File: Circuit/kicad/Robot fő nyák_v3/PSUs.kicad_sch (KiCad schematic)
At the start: 42 parts, among them U46 AP64501SP-13, U47 AP64501SP-13, U48 AP64501SP-13

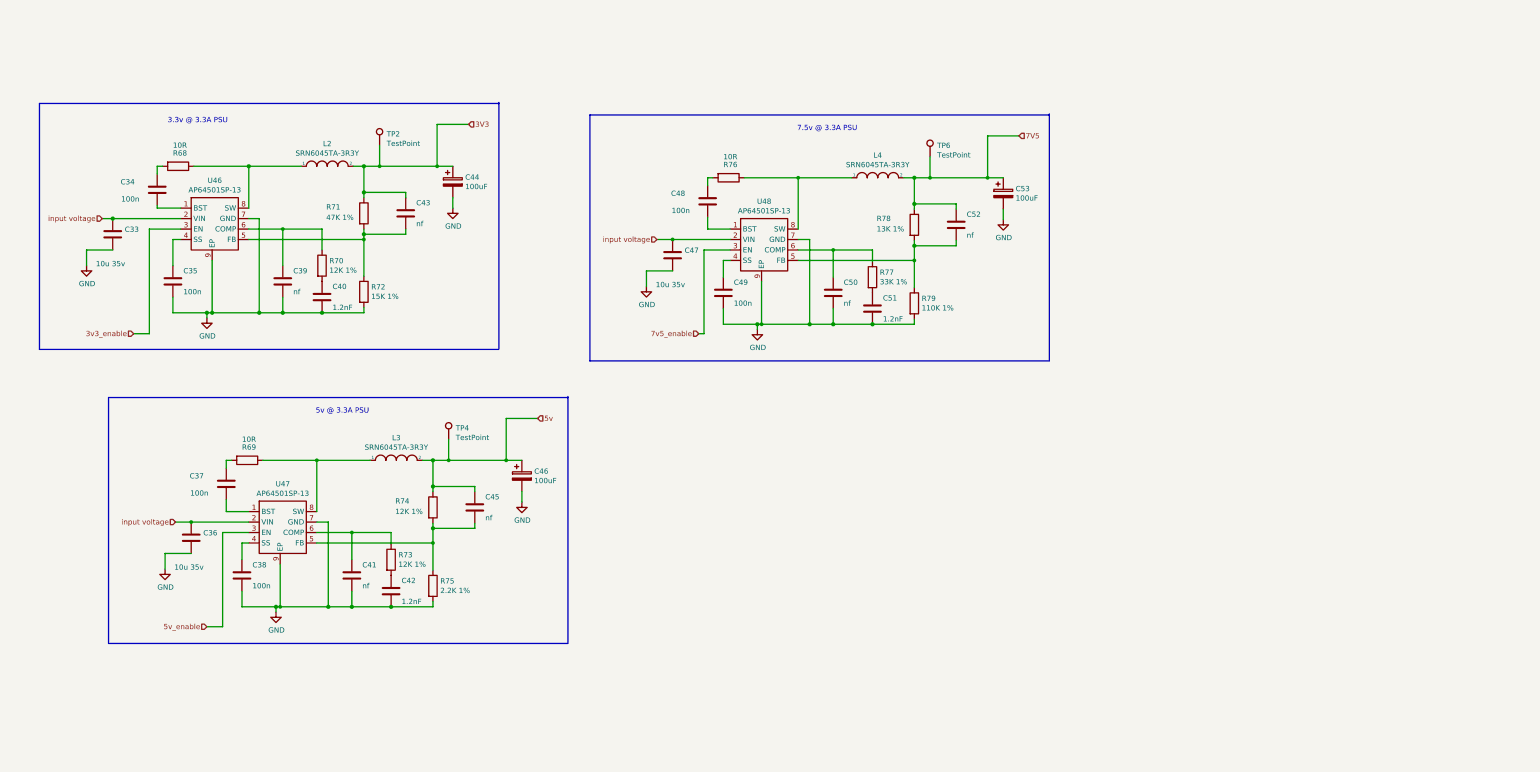
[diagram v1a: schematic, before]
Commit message: kicad bugfixs + bno085 + level shifter ics
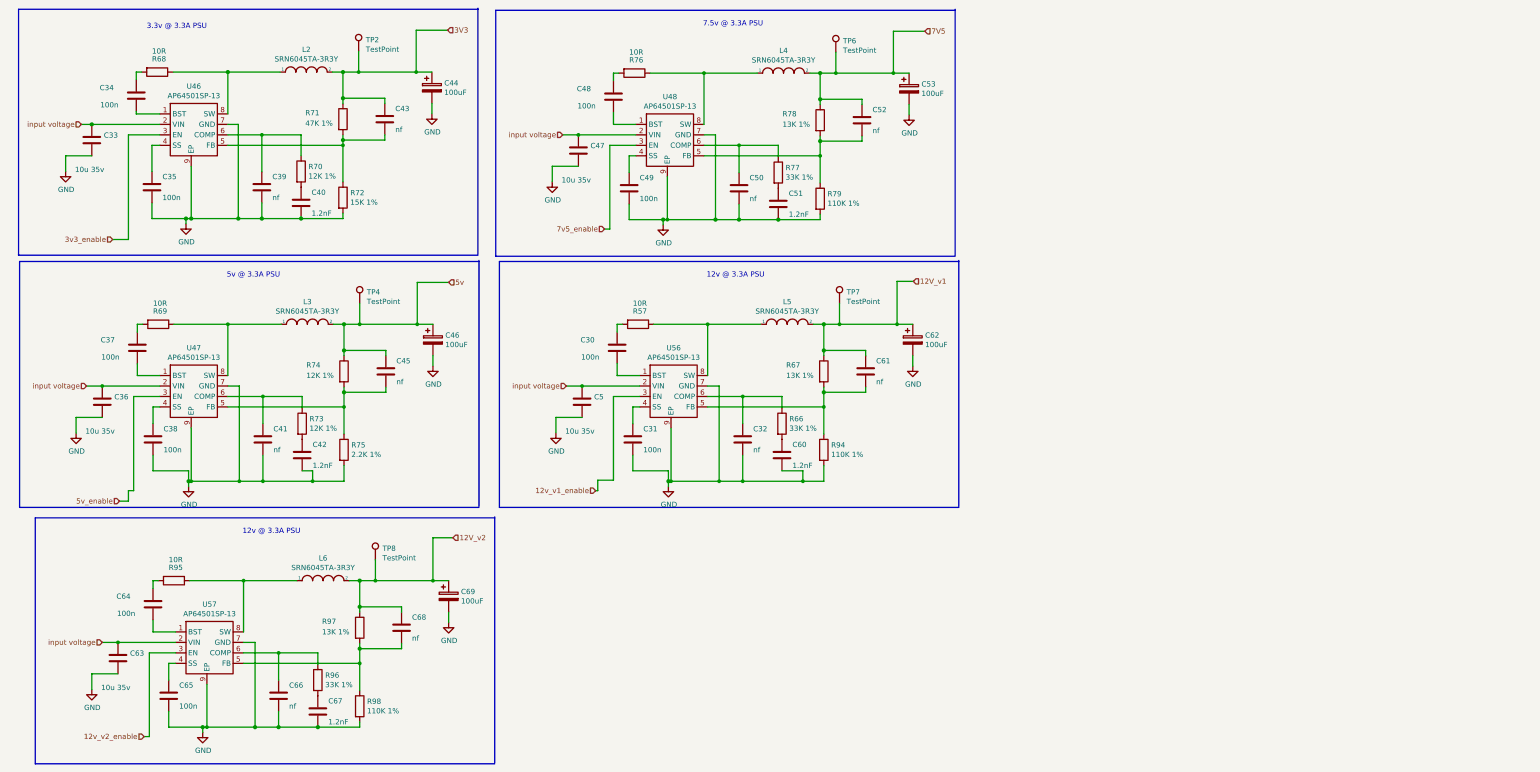
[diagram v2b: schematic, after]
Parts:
- added C30, C31, C64, C65: 100n, Capacitor_SMD:C_0805_2012Metric, symbol Device:C
- added C32, C61, C66, C68: nf, Capacitor_SMD:C_0805_2012Metric, symbol Device:C
- added C5, C63: 10u 35v, Capacitor_SMD:C_0805_2012Metric, symbol Device:C
- added C60, C67: 1.2nF, Capacitor_SMD:C_0805_2012Metric, symbol Device:C
- added C62, C69: 100uF, Capacitor_Tantalum_SMD:CP_EIA-7343-31_Kemet-D, symbol Device:CP
- added L5, L6: SRN6045TA-3R3Y, Inductor_SMD:L_Bourns_SRN6045TA, symbol pspice:INDUCTOR
- added R57, R95: 10R, Resistor_SMD:R_0805_2012Metric_Pad1.20x1.40mm_HandSolder, symbol Device:R
- added R66, R96: 33K 1%, Resistor_SMD:R_0805_2012Metric_Pad1.20x1.40mm_HandSolder, symbol Device:R
- added R67, R97: 13K 1%, Resistor_SMD:R_0805_2012Metric_Pad1.20x1.40mm_HandSolder, symbol Device:R
- added R94, R98: 110K 1%, Resistor_SMD:R_0805_2012Metric_Pad1.20x1.40mm_HandSolder, symbol Device:R
- added TP7, TP8: TestPoint, TestPoint:TestPoint_Pad_1.0x1.0mm, symbol Connector:TestPoint
- added U56, U57: AP64501SP-13, Package_SO:SOIC-8-1EP_3.9x4.9mm_P1.27mm_EP2.95x4.9mm_Mask2.71x3.4mm_ThermalVias, symbol CM4IO:AP64351
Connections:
- net GND: now also C31.2, C32.2, C5.2, C60.2, C62.2, C63.2, C65.2, C66.2, C67.2, C69.2, R94.2, R98.2, U56.7 (GND), U56.9 (EP), U57.7 (GND), U57.9 (EP)
- net input voltage: now also C5.1, C63.1, U56.2 (VIN), U57.2 (VIN)
- new net: L5.1, R57.1, U56.8 (SW)
- new net: C30.1, R57.2
- new net: C30.2, U56.1 (BST)
- new net: C31.1, U56.4 (SS)
- new net: C61.2, R67.2, R94.1, U56.5 (FB)
- new net: C32.1, R66.1, U56.6 (COMP)
- new net: L6.1, R95.1, U57.8 (SW)
- new net: C64.1, R95.2
- new net: C65.1, U57.4 (SS)
- new net: C64.2, U57.1 (BST)
- new net: C68.2, R97.2, R98.1, U57.5 (FB)
- new net: C66.1, R96.1, U57.6 (COMP)
- new net: C67.1, R96.2
- new net: C60.1, R66.2
- new net 12V_v1: C61.1, C62.1, L5.2, R67.1, TP7.1
- new net 12V_v2: C68.1, C69.1, L6.2, R97.1, TP8.1
- new net 12v_v1_enable: U56.3 (EN)
- new net 12v_v2_enable: U57.3 (EN)
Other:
- note added: "12v @ 3.3A PSU"
- moved on the sheet: C33, C34, C35, C36, C37, C38, C39, C40, C41, C42, C43, C44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

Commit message: KICAD V3.01 Cleaned sheets + update + szekér modell add
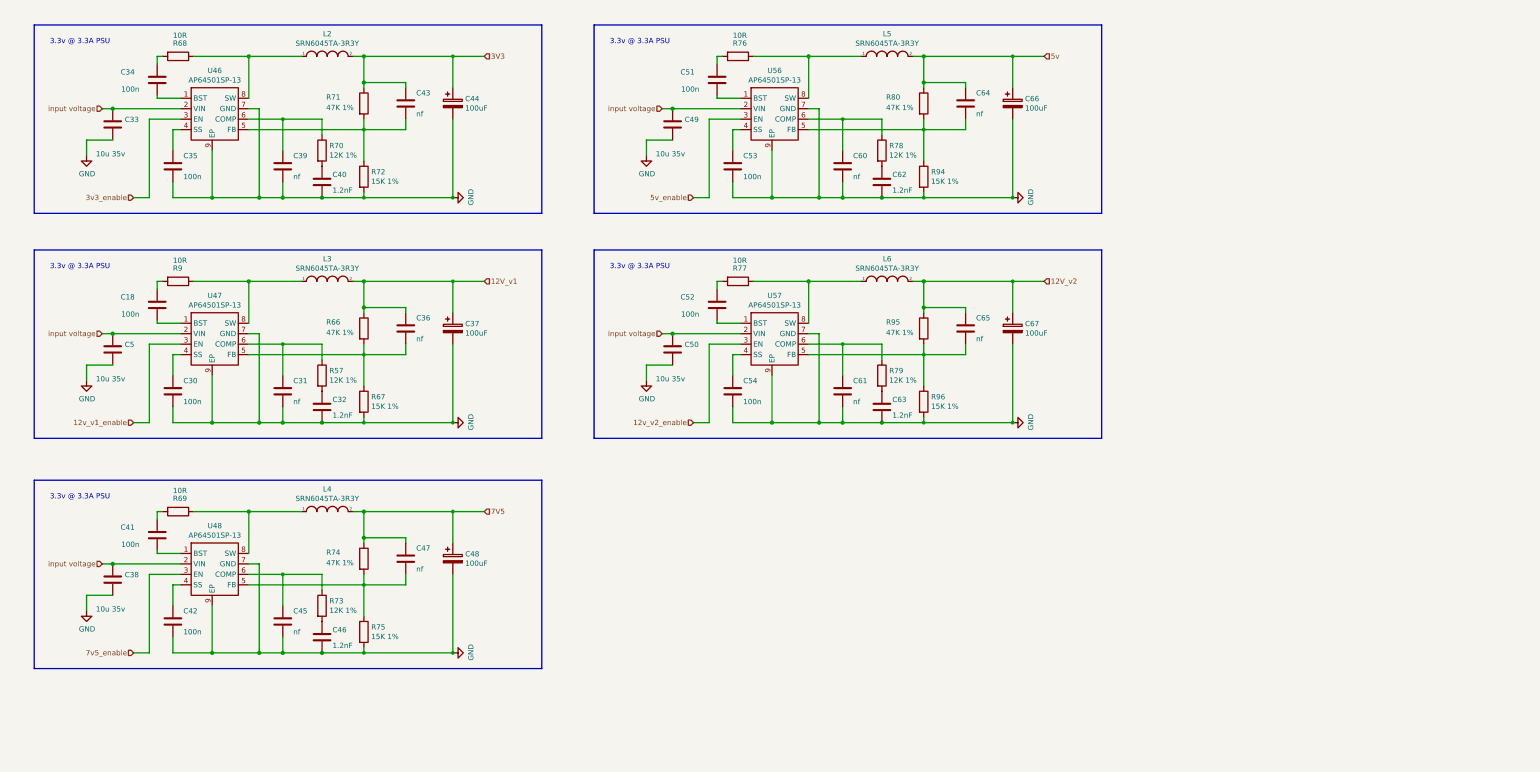
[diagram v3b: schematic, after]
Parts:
- removed C37, C48: 100n, Capacitor_SMD:C_0805_2012Metric, symbol Device:C
- removed C46, C53, C62, C69: 100uF, Capacitor_Tantalum_SMD:CP_EIA-7343-31_Kemet-D, symbol Device:CP
- removed C66, C68: nf, Capacitor_SMD:C_0805_2012Metric, symbol Device:C
- removed C67: 1.2nF, Capacitor_SMD:C_0805_2012Metric, symbol Device:C
- removed R97: 13K 1%, Resistor_SMD:R_0805_2012Metric_Pad1.20x1.40mm_HandSolder, symbol Device:R
- removed R98: 110K 1%, Resistor_SMD:R_0805_2012Metric_Pad1.20x1.40mm_HandSolder, symbol Device:R
- removed TP2, TP4, TP6, TP7, TP8: TestPoint, TestPoint:TestPoint_Pad_1.0x1.0mm, symbol Connector:TestPoint
- added C18, C53, C54: 100n, Capacitor_SMD:C_0805_2012Metric, symbol Device:C
- added C37, C48, C66, C67: 100uF, Capacitor_Tantalum_SMD:CP_EIA-7343-31_Kemet-D, symbol Device:CP
- added C46, C62: 1.2nF, Capacitor_SMD:C_0805_2012Metric, symbol Device:C
- added R80: 47K 1%, Resistor_SMD:R_0805_2012Metric_Pad1.20x1.40mm_HandSolder, symbol Device:R
- added R9: 10R, Resistor_SMD:R_0805_2012Metric_Pad1.20x1.40mm_HandSolder, symbol Device:R
- C31: value 100n -> nf; Field4 Farnell -> (none); Field5 2611911 -> (none); Field6 RM EMK105 B7104KV-F -> (none); Field7 TAIYO YUDEN EUROPE GMBH -> (none); Field8 110091611 -> (none); Part Description 0.1uF 10% 16V Ceramic Capacitor X7R 0402 (1005 Metric) -> (none)
- C32: value nf -> 1.2nF; Field4 (none) -> Digikey; Field5 (none) -> 490-16429-1-ND; Field6 (none) -> GCM155R71H122KA37D; Field7 (none) -> Murata; Part Description (none) -> 1200pF 10% 10V Ceramic Capacitor X5R 0402 (1005 Metric)
- C36, C47: value 10u 35v -> nf; Field5 490-10505-1-ND -> 490-17672-2-ND; Field6 GRM21BC8YA106KE11L -> GJM1555C1H270JB01D; Part Description 10uF 10% or 20% 35V Ceramic Capacitor X6S 0805 (2012 Metric) -> 27pF 5% 50V Ceramic Capacitor C0G, NP0 0402 (1005 Metric)
- C38, C49: value 100n -> 10u 35v; Field4 Farnell -> Digikey; Field5 2611911 -> 490-10505-1-ND; Field6 RM EMK105 B7104KV-F -> GRM21BC8YA106KE11L; Field7 TAIYO YUDEN EUROPE GMBH -> Murata; Field8 110091611 -> (none); Part Description 0.1uF 10% 16V Ceramic Capacitor X7R 0402 (1005 Metric) -> 10uF 10% or 20% 35V Ceramic Capacitor X6S 0805 (2012 Metric)
- C41: value nf -> 100n; Field4 (none) -> Farnell; Field5 (none) -> 2611911; Field6 (none) -> RM EMK105 B7104KV-F; Field7 (none) -> TAIYO YUDEN EUROPE GMBH; Field8 (none) -> 110091611; Part Description (none) -> 0.1uF 10% 16V Ceramic Capacitor X7R 0402 (1005 Metric)
- C42, C51: value 1.2nF -> 100n; Field4 Digikey -> Farnell; Field5 490-16429-1-ND -> 2611911; Field6 GCM155R71H122KA37D -> RM EMK105 B7104KV-F; Field7 Murata -> TAIYO YUDEN EUROPE GMBH; Field8 (none) -> 110091611; Part Description 1200pF 10% 10V Ceramic Capacitor X5R 0402 (1005 Metric) -> 0.1uF 10% 16V Ceramic Capacitor X7R 0402 (1005 Metric)
- C45, C61: Field4 Digikey -> (none); Field5 490-17672-2-ND -> (none); Field6 GJM1555C1H270JB01D -> (none); Field7 Murata -> (none); Part Description 27pF 5% 50V Ceramic Capacitor C0G, NP0 0402 (1005 Metric) -> (none)
- C50: value nf -> 10u 35v; Field4 (none) -> Digikey; Field5 (none) -> 490-10505-1-ND; Field6 (none) -> GRM21BC8YA106KE11L; Field7 (none) -> Murata; Part Description (none) -> 10uF 10% or 20% 35V Ceramic Capacitor X6S 0805 (2012 Metric)
- C52: value nf -> 100n; Field4 Digikey -> Farnell; Field5 490-17672-2-ND -> 2611911; Field6 GJM1555C1H270JB01D -> RM EMK105 B7104KV-F; Field7 Murata -> TAIYO YUDEN EUROPE GMBH; Field8 (none) -> 110091611; Part Description 27pF 5% 50V Ceramic Capacitor C0G, NP0 0402 (1005 Metric) -> 0.1uF 10% 16V Ceramic Capacitor X7R 0402 (1005 Metric)
- C60: value 1.2nF -> nf; Field4 Digikey -> (none); Field5 490-16429-1-ND -> (none); Field6 GCM155R71H122KA37D -> (none); Field7 Murata -> (none); Part Description 1200pF 10% 10V Ceramic Capacitor X5R 0402 (1005 Metric) -> (none)
- C63: value 10u 35v -> 1.2nF; Field5 490-10505-1-ND -> 490-16429-1-ND; Field6 GRM21BC8YA106KE11L -> GCM155R71H122KA37D; Part Description 10uF 10% or 20% 35V Ceramic Capacitor X6S 0805 (2012 Metric) -> 1200pF 10% 10V Ceramic Capacitor X5R 0402 (1005 Metric)
- C64, C65: value 100n -> nf; Field4 Farnell -> Digikey; Field5 2611911 -> 490-17672-2-ND; Field6 RM EMK105 B7104KV-F -> GJM1555C1H270JB01D; Field7 TAIYO YUDEN EUROPE GMBH -> Murata; Field8 110091611 -> (none); Part Description 0.1uF 10% 16V Ceramic Capacitor X7R 0402 (1005 Metric) -> 27pF 5% 50V Ceramic Capacitor C0G, NP0 0402 (1005 Metric)
- R57: value 10R -> 12K 1%; Field5 9238999 -> 9239367; Field6 RC0402FR-0710RL -> MCR01MZPF1202; Field7 Yageo -> Rohm; Field8 URES00256 -> (none); Part Description Resistor 10R M1005 1% 63mW -> Resistor 12K M1005 1% 63mW
- R66: value 33K 1% -> 47K 1%; Field5 9239367 -> 9239430; Field6 MCR01MZPF1202 -> RK73G1ETQTP4702D; Field7 Rohm -> KOA EUROPE GMBH; Field8 (none) -> 120892781; Part Description Resistor 12K M1005 1% 63mW -> Resistor 47K M1005 1% 63mW
- R67: value 13K 1% -> 15K 1%; Field5 9239430 -> 9239375; Field6 RK73G1ETQTP4702D -> MCR01MZPF1502; Field7 KOA EUROPE GMBH -> Rohm; Field8 120892781 -> 120891581; Part Description Resistor 47K M1005 1% 63mW -> Resistor 15K M1005 1% 63mW
- R74: value 12K 1% -> 47K 1%
- R75: value 2.2K 1% -> 15K 1%
- R77: value 33K 1% -> 10R; Field5 9239367 -> 9238999; Field6 MCR01MZPF1202 -> RC0402FR-0710RL; Field7 Rohm -> Yageo; Field8 (none) -> URES00256; Part Description Resistor 12K M1005 1% 63mW -> Resistor 10R M1005 1% 63mW
- R78: value 13K 1% -> 12K 1%; Field5 9239430 -> 9239367; Field6 RK73G1ETQTP4702D -> MCR01MZPF1202; Field7 KOA EUROPE GMBH -> Rohm; Field8 120892781 -> (none); Part Description Resistor 47K M1005 1% 63mW -> Resistor 12K M1005 1% 63mW
- R79: value 110K 1% -> 12K 1%; Field5 9239375 -> 9239367; Field6 MCR01MZPF1502 -> MCR01MZPF1202; Field8 120891581 -> (none); Part Description Resistor 15K M1005 1% 63mW -> Resistor 12K M1005 1% 63mW
- R94: value 110K 1% -> 15K 1%
- R95: value 10R -> 47K 1%; Field5 9238999 -> 9239430; Field6 RC0402FR-0710RL -> RK73G1ETQTP4702D; Field7 Yageo -> KOA EUROPE GMBH; Field8 URES00256 -> 120892781; Part Description Resistor 10R M1005 1% 63mW -> Resistor 47K M1005 1% 63mW
- R96: value 33K 1% -> 15K 1%; Field5 9239367 -> 9239375; Field6 MCR01MZPF1202 -> MCR01MZPF1502; Field8 (none) -> 120891581; Part Description Resistor 12K M1005 1% 63mW -> Resistor 15K M1005 1% 63mW
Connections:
- net 12V_v1: now also C36.1, L3.2, R66.1, C37.1; no longer C61.1, L5.2, R67.1
- net 12V_v2: now also C65.1, R95.1, C67.1
- net 12v_v1_enable: now also U47.3 (EN); no longer U56.3 (EN)
- net 5v: now also C64.1, L5.2, C66.1, R80.1; no longer C45.1, L3.2, R74.1
- net 5v_enable: now also U56.3 (EN); no longer U47.3 (EN)
- net 7V5: now also C47.1, R74.1, C48.1; no longer C52.1, R78.1
- net GND: now also C30.2, C45.2, C61.2, R67.2, R96.2, C37.2, C46.2, C48.2, C53.2, C54.2, C62.2, C66.2, C67.2; no longer C36.2, C41.2, C47.2, C51.2, C65.2, R79.2
- net input voltage: now also C38.1, C49.1, C50.1; no longer C36.1, C47.1, C63.1
- net at L3.1, U47.8 (SW): now also R9.1; no longer R69.1
- net at R69.2: now also C41.1
- net at U48.1 (BST): now also C41.2
- net at U48.4 (SS): now also C42.1; no longer C49.1
- net at L4.1, U48.8 (SW): now also R69.1; no longer R76.1
- net at R74.2, R75.1: now also C47.2, U48.5 (FB); no longer C45.2, U47.5 (FB)
- net at U47.1 (BST): now also C18.2
- net at L5.1, U56.8 (SW): now also R76.1; no longer R57.1
- net at C30.1: now also U47.4 (SS); no longer R57.2
- net at U56.1 (BST): now also C51.2; no longer C30.2
- net at U56.4 (SS): now also C53.1; no longer C31.1
- net at R94.1, U56.5 (FB): now also C64.2, R80.2; no longer C61.2, R67.2
- net at L6.1, U57.8 (SW): now also R77.1; no longer R95.1
- net at R95.2: now also C65.2, R96.1, U57.5 (FB); no longer C64.1
- net at R77.2: now also C52.1; no longer C51.1
- net at U57.4 (SS): now also C54.1; no longer C65.1
- net at U57.1 (BST): now also C52.2; no longer C64.2
- net at U57.6 (COMP): now also C61.1, R79.1; no longer R96.1
- net at R76.2: now also C51.1
- net at R73.2: now also C46.1; no longer C42.1
- net at R66.2: now also C36.2, R67.1, U47.5 (FB); no longer C60.1
- new net: C45.1, R73.1, U48.6 (COMP)
- new net: C18.1, R9.2
- new net: C62.1, R78.2
- new net: C63.1, R79.2
- new net: C60.1, R78.1, U56.6 (COMP)
- new net: C31.1, R57.1, U47.6 (COMP)
- new net: C32.1, R57.2
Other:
- note removed: "12v @ 3.3A PSU"
- note removed: "5v @ 3.3A PSU"
- note removed: "7.5v @ 3.3A PSU"
- moved on the sheet: C33, C34, C35, C39, C40, C43, C44, L2, R68, R70, R71, R72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

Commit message: kicad v0.1 footprint- assing spi finish
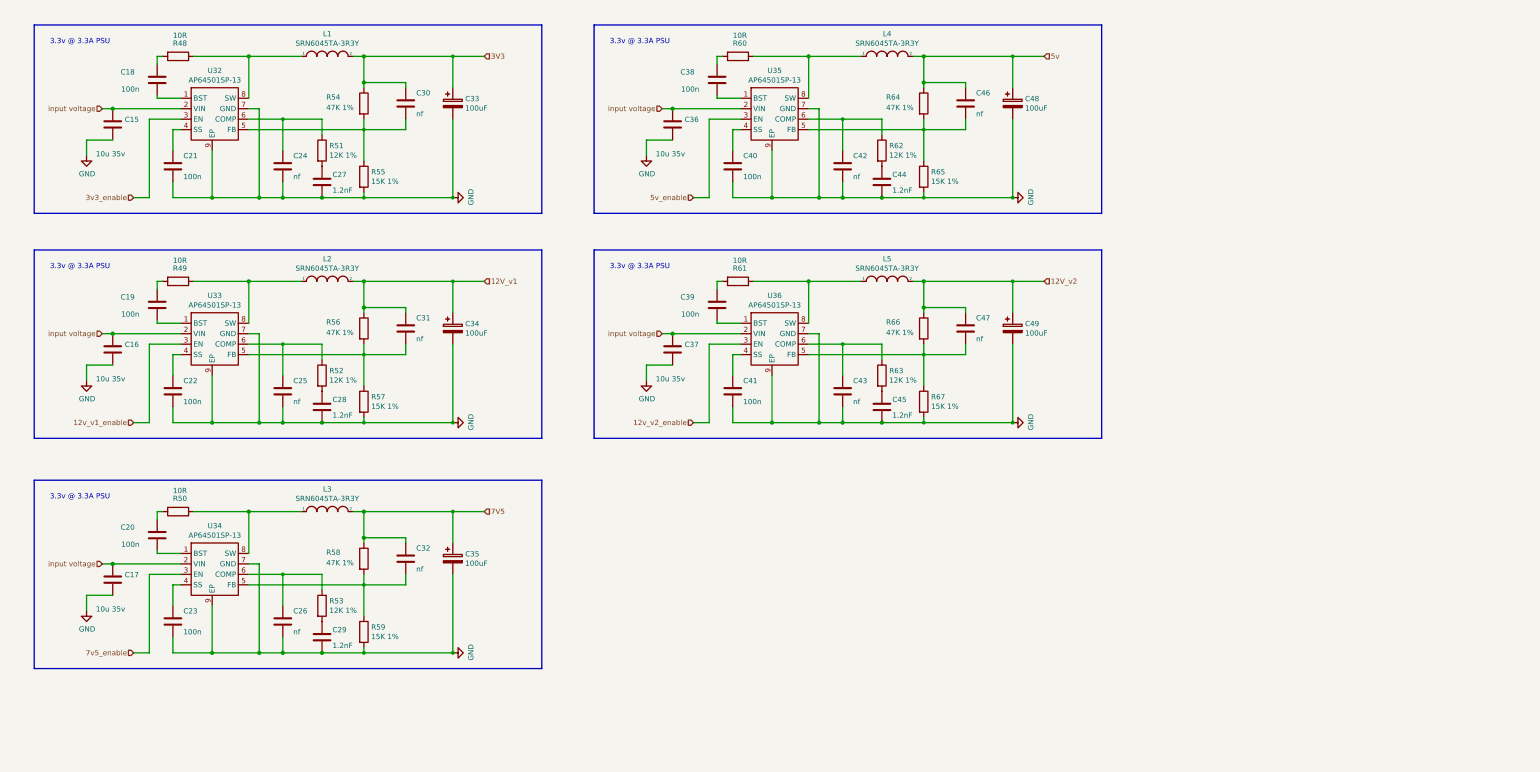
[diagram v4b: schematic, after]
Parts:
- R48: renamed from R68; footprint Resistor_SMD:R_0805_2012Metric_Pad1.20x1.40mm_HandSolder -> Resistor_SMD:R_0805_2012Metric
- R49: renamed from R9; footprint Resistor_SMD:R_0805_2012Metric_Pad1.20x1.40mm_HandSolder -> Resistor_SMD:R_0805_2012Metric
- R50: renamed from R69; footprint Resistor_SMD:R_0805_2012Metric_Pad1.20x1.40mm_HandSolder -> Resistor_SMD:R_0805_2012Metric
- R51: renamed from R70; footprint Resistor_SMD:R_0805_2012Metric_Pad1.20x1.40mm_HandSolder -> Resistor_SMD:R_0805_2012Metric
- R52: renamed from R57; footprint Resistor_SMD:R_0805_2012Metric_Pad1.20x1.40mm_HandSolder -> Resistor_SMD:R_0805_2012Metric
- R53: renamed from R73; footprint Resistor_SMD:R_0805_2012Metric_Pad1.20x1.40mm_HandSolder -> Resistor_SMD:R_0805_2012Metric
- R54: renamed from R71; footprint Resistor_SMD:R_0805_2012Metric_Pad1.20x1.40mm_HandSolder -> Resistor_SMD:R_0805_2012Metric
- R55: renamed from R72; footprint Resistor_SMD:R_0805_2012Metric_Pad1.20x1.40mm_HandSolder -> Resistor_SMD:R_0805_2012Metric
- R56: renamed from R66; footprint Resistor_SMD:R_0805_2012Metric_Pad1.20x1.40mm_HandSolder -> Resistor_SMD:R_0805_2012Metric
- R57: renamed from R67; footprint Resistor_SMD:R_0805_2012Metric_Pad1.20x1.40mm_HandSolder -> Resistor_SMD:R_0805_2012Metric
- R58: renamed from R74; footprint Resistor_SMD:R_0805_2012Metric_Pad1.20x1.40mm_HandSolder -> Resistor_SMD:R_0805_2012Metric
- R59: renamed from R75; footprint Resistor_SMD:R_0805_2012Metric_Pad1.20x1.40mm_HandSolder -> Resistor_SMD:R_0805_2012Metric
- R60: renamed from R76; footprint Resistor_SMD:R_0805_2012Metric_Pad1.20x1.40mm_HandSolder -> Resistor_SMD:R_0805_2012Metric
- R61: renamed from R77; footprint Resistor_SMD:R_0805_2012Metric_Pad1.20x1.40mm_HandSolder -> Resistor_SMD:R_0805_2012Metric
- R62: renamed from R78; footprint Resistor_SMD:R_0805_2012Metric_Pad1.20x1.40mm_HandSolder -> Resistor_SMD:R_0805_2012Metric
- R63: renamed from R79; footprint Resistor_SMD:R_0805_2012Metric_Pad1.20x1.40mm_HandSolder -> Resistor_SMD:R_0805_2012Metric
- R64: renamed from R80; footprint Resistor_SMD:R_0805_2012Metric_Pad1.20x1.40mm_HandSolder -> Resistor_SMD:R_0805_2012Metric
- R65: renamed from R94; footprint Resistor_SMD:R_0805_2012Metric_Pad1.20x1.40mm_HandSolder -> Resistor_SMD:R_0805_2012Metric
- R66: renamed from R95; footprint Resistor_SMD:R_0805_2012Metric_Pad1.20x1.40mm_HandSolder -> Resistor_SMD:R_0805_2012Metric
- R67: renamed from R96; footprint Resistor_SMD:R_0805_2012Metric_Pad1.20x1.40mm_HandSolder -> Resistor_SMD:R_0805_2012Metric
- renumbered C33 to C15, C5 to C16, C38 to C17, C34 to C18, C18 to C19, C41 to C20, C35 to C21, C30 to C22, C42 to C23, C39 to C24, C31 to C25, C45 to C26, C40 to C27, C32 to C28, C46 to C29, C43 to C30, C36 to C31, C47 to C32, C44 to C33, C37 to C34, C48 to C35, C49 to C36, C50 to C37, C51 to C38, C52 to C39, C53 to C40, C54 to C41, C60 to C42, C61 to C43, C62 to C44, C63 to C45, C64 to C46, C65 to C47, C66 to C48, C67 to C49, L2 to L1, L3 to L2, L4 to L3, L5 to L4, L6 to L5, U46 to U32, U47 to U33, U48 to U34, U56 to U35, U57 to U36

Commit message: kicad update new readme media updates the circuit is 95% finished
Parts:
- added C108, C109, C110, C111, C112: 1uf, Capacitor_SMD:C_0805_2012Metric, symbol Device:C
- C33, C34, C35, C48, C49: value 100uF -> 470uf
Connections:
- net 12V_v1: now also C109.1
- net 12V_v2: now also C111.1
- net 3V3: now also C110.1
- net 5v: now also C112.1
- net 7V5: now also C108.1
- net GND: now also C108.2, C109.2, C110.2, C111.2, C112.2
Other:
- moved on the sheet: C35

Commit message: readme updated kicad circuit V1
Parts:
- removed C15, C16, C17, C36, C37: 10u 35v, Capacitor_SMD:C_0805_2012Metric, symbol Device:C
- added TP12, TP13, TP14, TP15, TP16: TestPoint, TestPoint:TestPoint_Pad_D2.0mm, symbol Connector:TestPoint
- C56: renamed from C35; footprint Capacitor_Tantalum_SMD:CP_EIA-7343-31_Kemet-D -> Capacitor_SMD:CP_Elec_8x10
- C57: renamed from C33; footprint Capacitor_Tantalum_SMD:CP_EIA-7343-31_Kemet-D -> Capacitor_SMD:CP_Elec_8x10
- C58: renamed from C34; footprint Capacitor_Tantalum_SMD:CP_EIA-7343-31_Kemet-D -> Capacitor_SMD:CP_Elec_8x10
- C74: renamed from C48; footprint Capacitor_Tantalum_SMD:CP_EIA-7343-31_Kemet-D -> Capacitor_SMD:CP_Elec_8x10
- C75: renamed from C49; footprint Capacitor_Tantalum_SMD:CP_EIA-7343-31_Kemet-D -> Capacitor_SMD:CP_Elec_8x10
- renumbered C18 to C41, C19 to C42, C20 to C43, C21 to C44, C22 to C45, C23 to C46, C24 to C47, C25 to C48, C26 to C49, C27 to C50, C28 to C51, C29 to C52, C30 to C53, C31 to C54, C32 to C55, C110 to C59, C109 to C60, C108 to C61, C38 to C64, C39 to C65, C40 to C66, C41 to C67, C42 to C68, C43 to C69, C44 to C70, C45 to C71, C46 to C72, C47 to C73, C112 to C76, C111 to C77, R48 to R49, R49 to R50, R50 to R51, R51 to R52, R52 to R53, R53 to R54, R54 to R55, R55 to R56, R56 to R57, R57 to R58, R58 to R59, R59 to R60, R60 to R61, R61 to R62, R62 to R63, R63 to R64, R64 to R65, R65 to R66, R66 to R67, R67 to R68, U32 to U31, U33 to U32, U34 to U33, U35 to U34, U36 to U35
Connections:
- net 12V_v1: now also TP15.1
- net 12V_v2: now also TP14.1
- net 3V3: now also TP12.1
- net 5v: now also TP13.1
- net 7V5: now also TP16.1

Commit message: kicad update
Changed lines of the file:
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@@
+	(wire
+		(pts
+			(xy 267.97 74.93) (xy 267.97 80.01)
+		)
+		(stroke
+			(width 0)
+			(type solid)
+		)
+	)
 	(wire
 		(pts
@@
 	(wire
 		(pts
-			(xy 267.97 80.01) (xy 269.24 80.01)
+			(xy 267.97 74.93) (xy 269.24 74.93)
 		)
 		(stroke
@@
 	(wire
 		(pts
+			(xy 130.81 76.2) (xy 130.81 80.01)
+		)
+		(stroke
+			(width 0)
+			(type solid)
+		)
+	)
+	(wire
+		(pts
 			(xy 224.79 114.3) (xy 234.95 114.3)
 		)
@@
 		(pts
 			(xy 99.06 25.4) (xy 106.68 25.4)
-		)
-		(stroke
-			(width 0)
-			(type solid)
-		)
-	)
-	(wire
-		(pts
-			(xy 130.81 80.01) (xy 132.08 80.01)
 		)
 		(stroke
@@
 	(hierarchical_label "12V_v1"
 		(shape input)
-		(at 132.08 80.01 0)
+		(at 130.81 76.2 0)
 		(effects
 			(font
@@
 	(hierarchical_label "12V_v2"
 		(shape input)
-		(at 269.24 80.01 0)
+		(at 269.24 74.93 0)
 		(effects
 			(font
